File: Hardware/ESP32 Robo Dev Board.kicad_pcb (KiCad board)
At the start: 4 copper layers, 60 x 60 mm, 67 parts, among them J1 USB_C_Receptacle_USB2.0, J2 Conn_01x02_Pin, Q1 DMP2045U, SW1 SW_Push_Dual_x2, U1 ESP32-S3-WROOM-1, U2 TCA9548ARGER, U4 STSPIN250, U5 STSPIN250, U6 USBLC6-2P6, U8 MCP73831-2-OT, U9 AP2112K-3.3

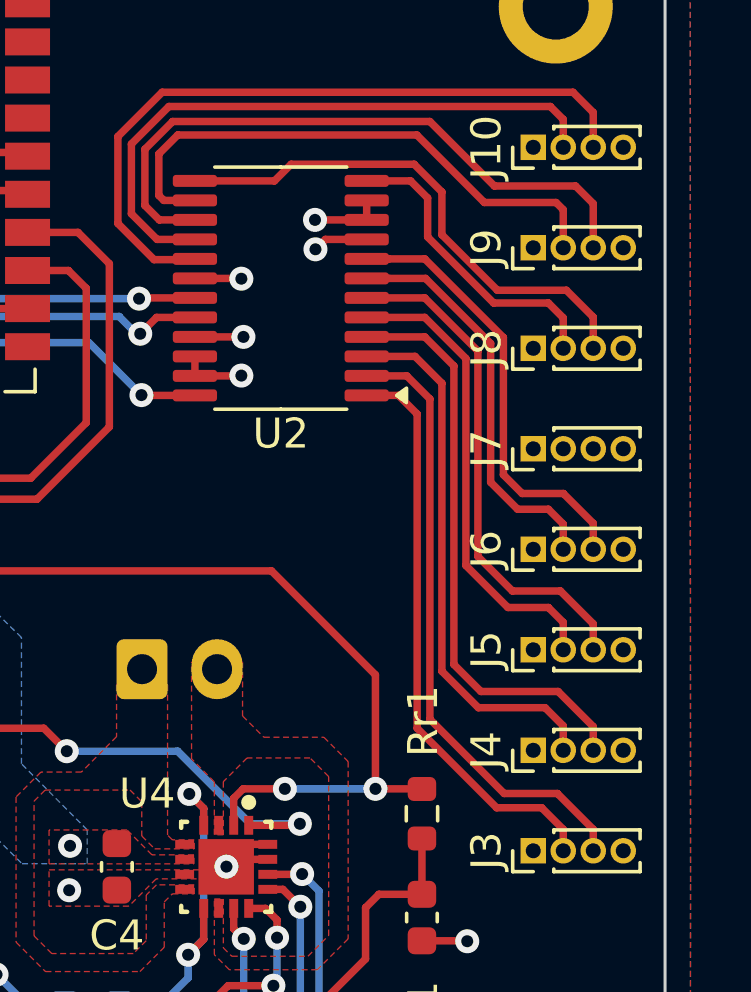
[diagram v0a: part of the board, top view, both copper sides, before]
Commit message: Update I2C Bus Connections
Channel 4 of I2C was not connected, will make traces pretty later.
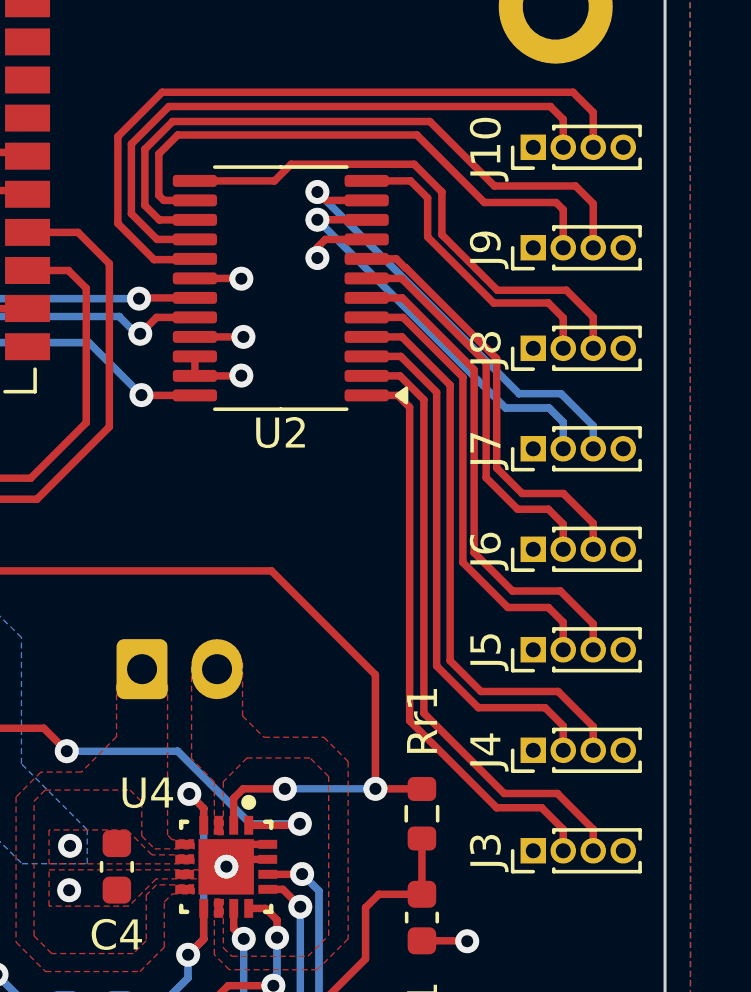
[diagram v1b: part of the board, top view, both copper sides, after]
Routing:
- net /I2C_4C: track 0.00 -> 14.9 mm, vias 0 -> 1
- net /I2C_4D: track 0.00 -> 13.5 mm, vias 0 -> 1
- net GND: track 85.7 -> 83.6 mm, vias 39 -> 38
- net /I2C_3C: track 15.5 -> 14.9 mm

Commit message: Tweaked n' fixed things with @Amoskeag
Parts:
- added Rs2: 18 KΩ, Resistor_SMD:R_0603_1608Metric, F.Cu at (174.2, 81.5)
- added Rs3: 100, Resistor_SMD:R_0603_1608Metric, F.Cu at (174.2, 79.5)
- added SW2: SW_Push, Button_Switch_THT:SW_TH_Tactile_Omron_B3F-100x, F.Cu at (164.5, 78.5)
- moved REF** 42.7 mm to (173.5, 75.0)
- moved G*** 3.45 mm to (152.6, 117.2)
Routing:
- net /Boot: track 0.00 -> 25.8 mm, vias 0 -> 1
- net Net-(Rs3-Pad1): track 0.00 -> 9.64 mm
- net /R_Signal_A: track 2.04 -> 0.00 mm, vias 1 -> 0
- net /R_Signal_B: track 2.00 -> 0.00 mm, vias 1 -> 0
- net /VBAT_DET: track 34.2 -> 35.7 mm
- net GND: vias 38 -> 39
- net +3V3: vias 4 -> 5
- added copper zone on In1.Cu, net +3V3
- removed copper zone on B.Cu, net (none)
- removed copper zone on F.Cu, net (none)

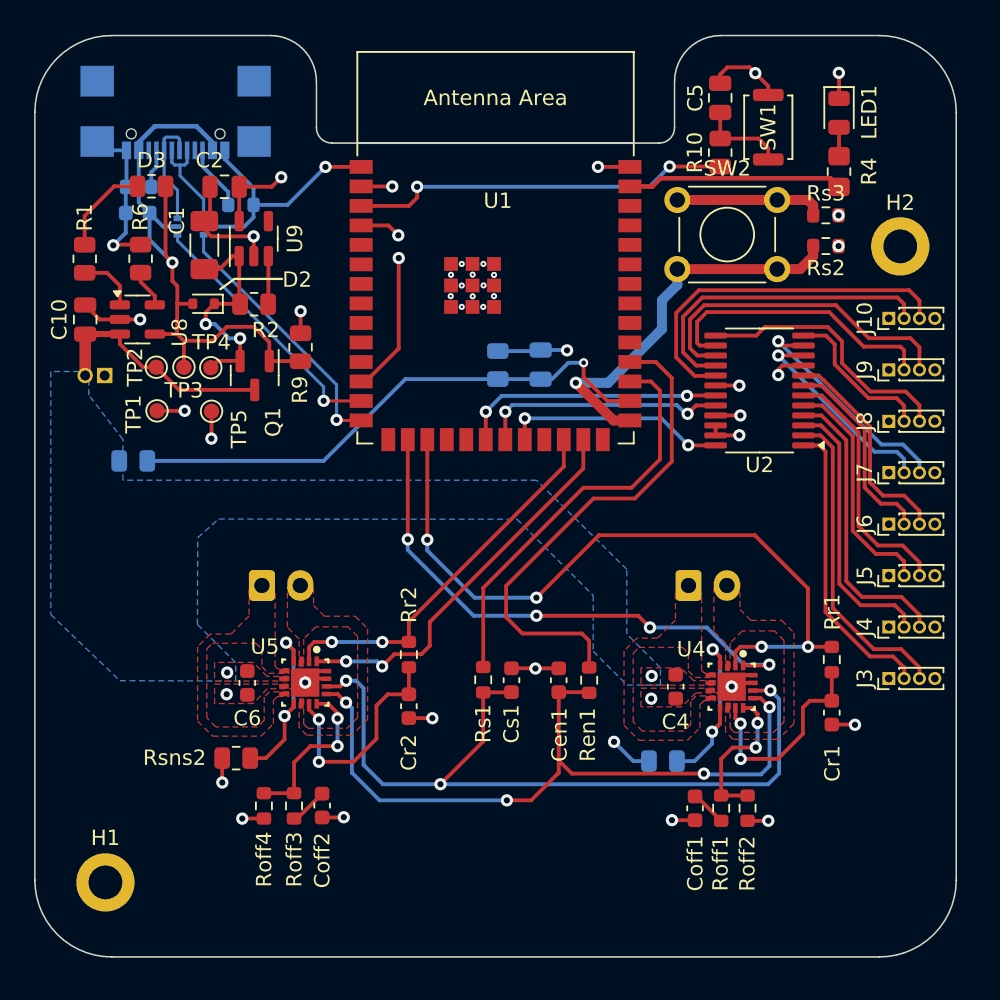
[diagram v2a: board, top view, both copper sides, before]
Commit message: Fix Footprint Targets
Fixed DRC errors on footprints.
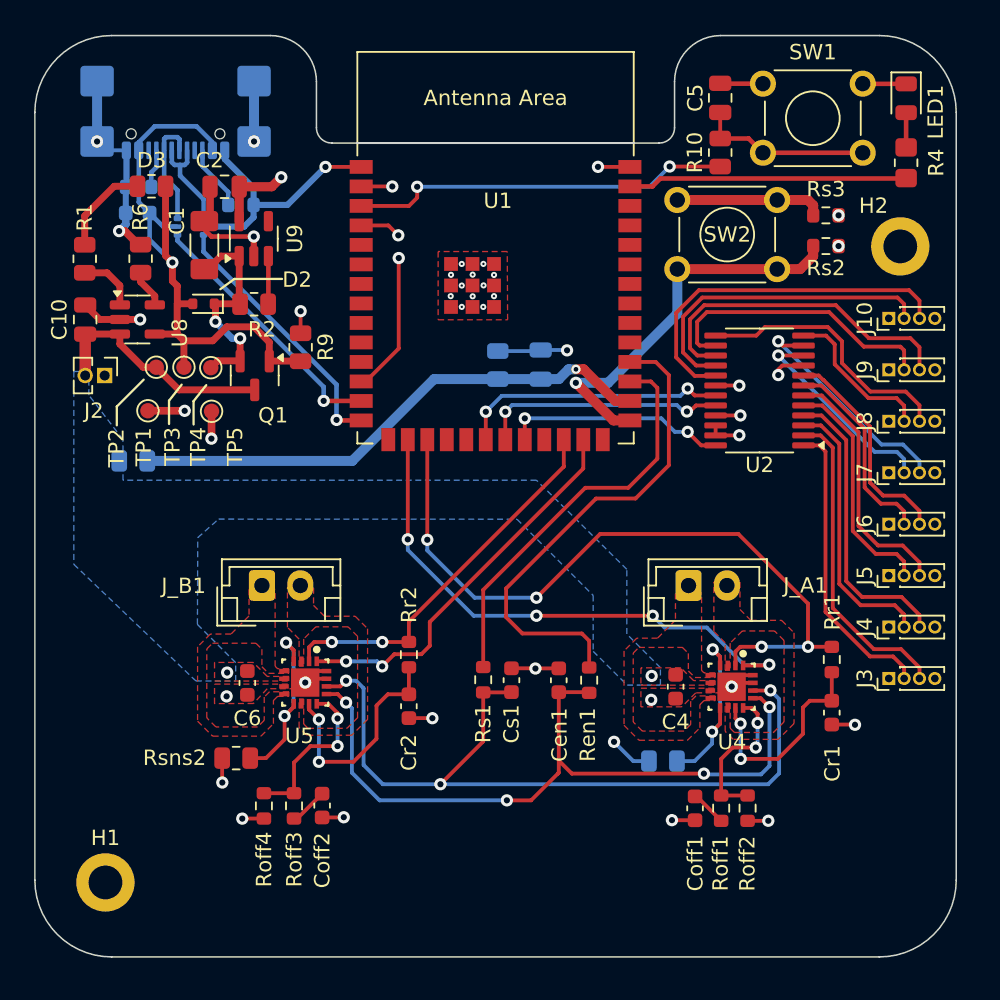
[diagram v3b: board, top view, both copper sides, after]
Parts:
- J1: footprint Amoskeag_KiCAD_Lib:GCT_USB4110GFA -> Connector_USB:USB_C_Receptacle_GCT_USB4110
- J2, J_A1, J_B1: moved to F.Cu
- SW1: footprint Button_Switch_SMD:SW_Push_SPST_NO_Alps_SKRK -> Button_Switch_THT:SW_TH_Tactile_Omron_B3F-100x
- moved REF** 47.1 mm to (176.9, 122.0)
- moved LED1 4.47 mm to (179.4, 71.9)
- moved R4 4.41 mm to (179.4, 76.1)
- moved SW1 2.86 mm to (170.1, 70.9), turned to 0 degrees
- moved J1 2.61 mm to (131.8, 71.6)
- moved G*** 1.82 mm to (152.9, 115.4)
- moved TP1 0.60 mm to (130.0, 92.2)
- turned J2 to -90 degrees
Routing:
- net GND: track 83.6 -> 89.4 mm
- net Net-(SW1A-D): track 5.81 -> 11.4 mm
- net /GPIO1: track 14.1 -> 18.3 mm
- net /VBAT_DET: track 35.7 -> 34.8 mm
- net /V_IN: track 15.2 -> 14.4 mm
- net +3V3: track 10.7 -> 11.3 mm
- net /PWM A: track 47.5 -> 47.0 mm

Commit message: Add JST Connectors for Encoders
Added JST Connectors for my Encoders to attach to.

Fixed all DRC Errors.
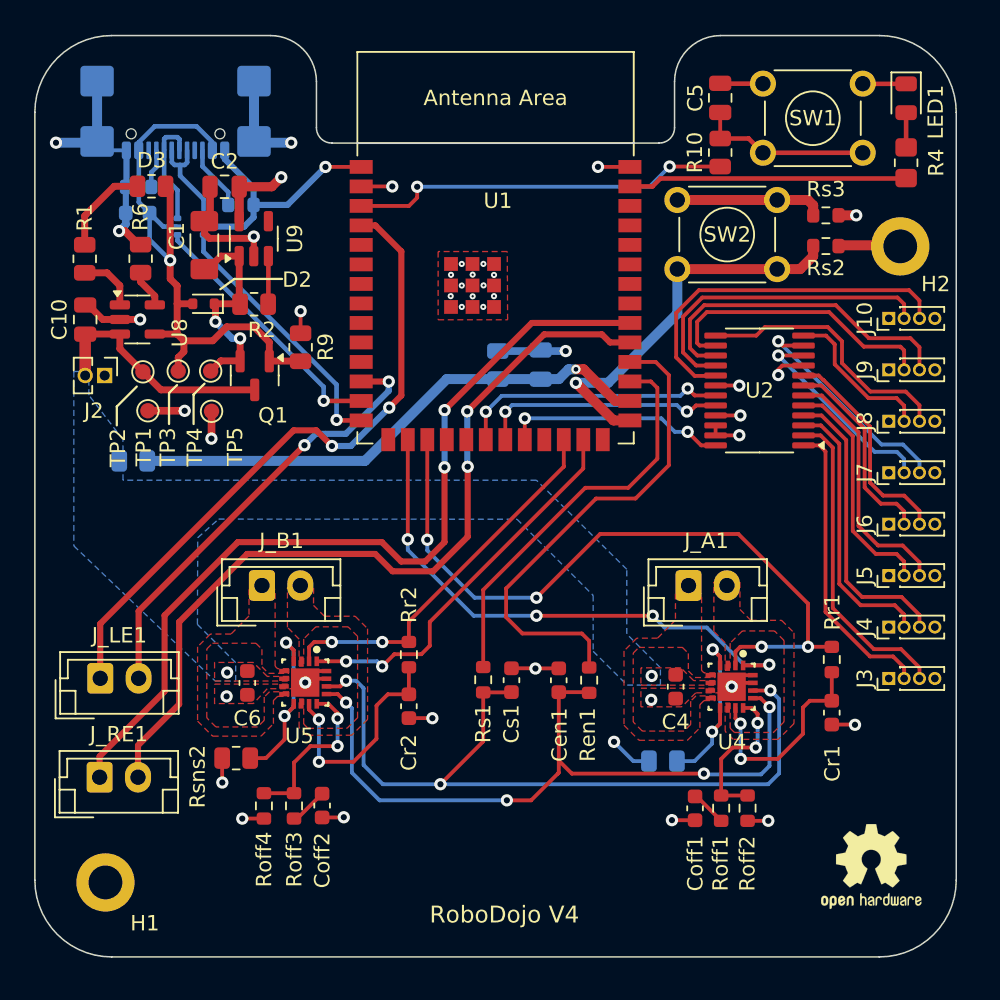
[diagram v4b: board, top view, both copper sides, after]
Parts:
- added J_LE1: Left Encoder, Connector_JST:JST_EH_B2B-EH-A_1x02_P2.50mm_Vertical, F.Cu at (126.9, 109.7)
- added J_RE1: Right Encoder, Connector_JST:JST_EH_B2B-EH-A_1x02_P2.50mm_Vertical, F.Cu at (126.9, 116.1)
- REF**: moved to F.Cu
- moved TP2 0.92 mm to (129.7, 89.7)
- moved TP3 0.45 mm to (132.0, 89.6)
- moved REF** 0.25 mm to (177.1, 121.9), turned to 0 degrees
- moved TP4 0.22 mm to (134.1, 89.6)
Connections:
- U1 pad 31: /R_Signal_B -> /R_Signal_A
- U1 pad 32: /R_Signal_A -> /R_Signal_B
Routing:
- net /R_Signal_B: track 0.00 -> 56.6 mm, vias 0 -> 2
- net /R_Signal_A: track 0.00 -> 54.6 mm, vias 0 -> 2
- net /L_Signal_B: track 2.68 -> 42.9 mm, vias 1 -> 2
- net /L_Signal_A: track 9.23 -> 29.0 mm, vias 1 -> 2
- net GND: track 89.4 -> 98.8 mm, vias 39 -> 38
- net +3V3: track 11.3 -> 12.4 mm
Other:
- board text added: "RoboDojo V4"
- board text removed: "Design By Arthur W. Aznive Jr. https://github.com/Amoskeag/RoboDojo"

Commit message: Increase Trace Widths
Increased the smallest trace width from 0.25 mm to 0.3 mm and beefed up all the other traces.
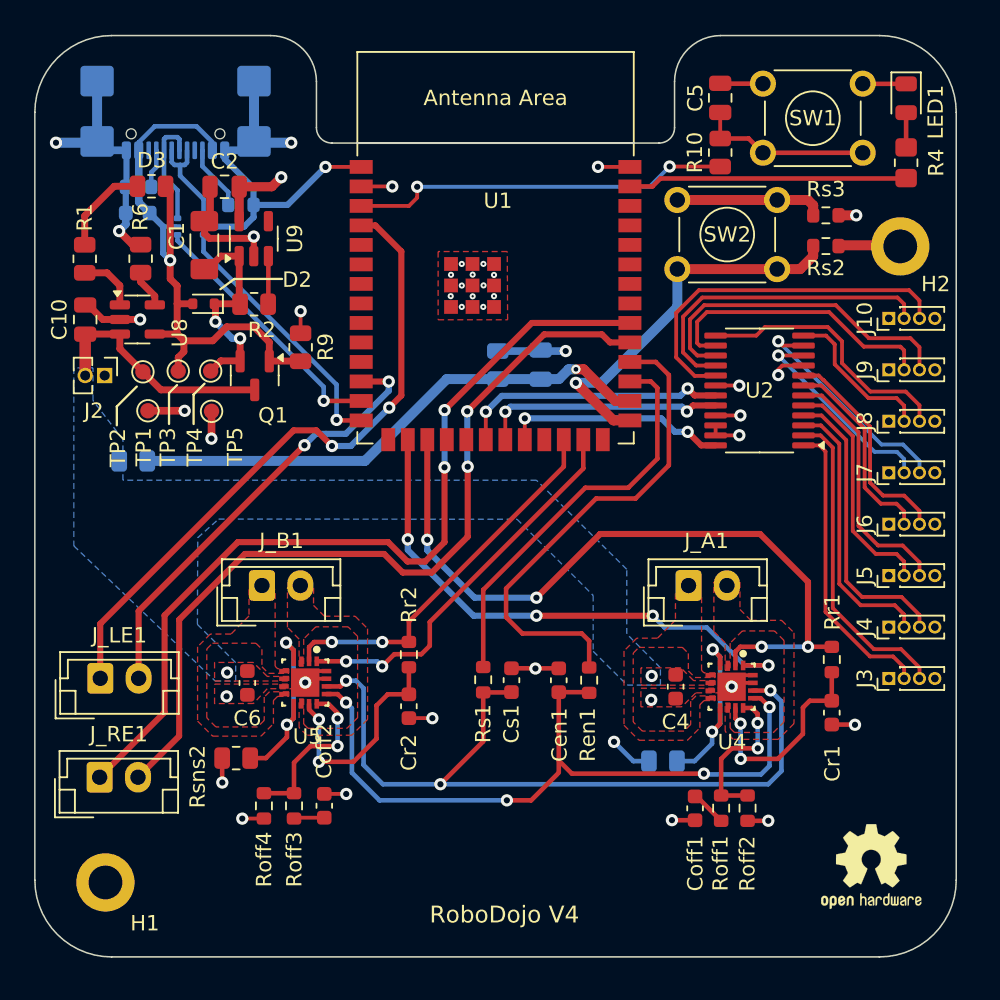
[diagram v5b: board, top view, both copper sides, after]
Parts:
- SW1: value SW_Push_Dual_x2 -> SW1
- moved Coff2 0.14 mm to (141.5, 118.0), turned to 90 degrees
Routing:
- net GND: track 98.8 -> 101.0 mm
- net /V_BUS: track 41.7 -> 40.5 mm
- net /PWM A: track 47.0 -> 47.9 mm
- net /Motor Controller Right/SENSE: track 12.0 -> 12.5 mm

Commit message: Clean Up Schematic
Fixed Schematic notes, and formatting
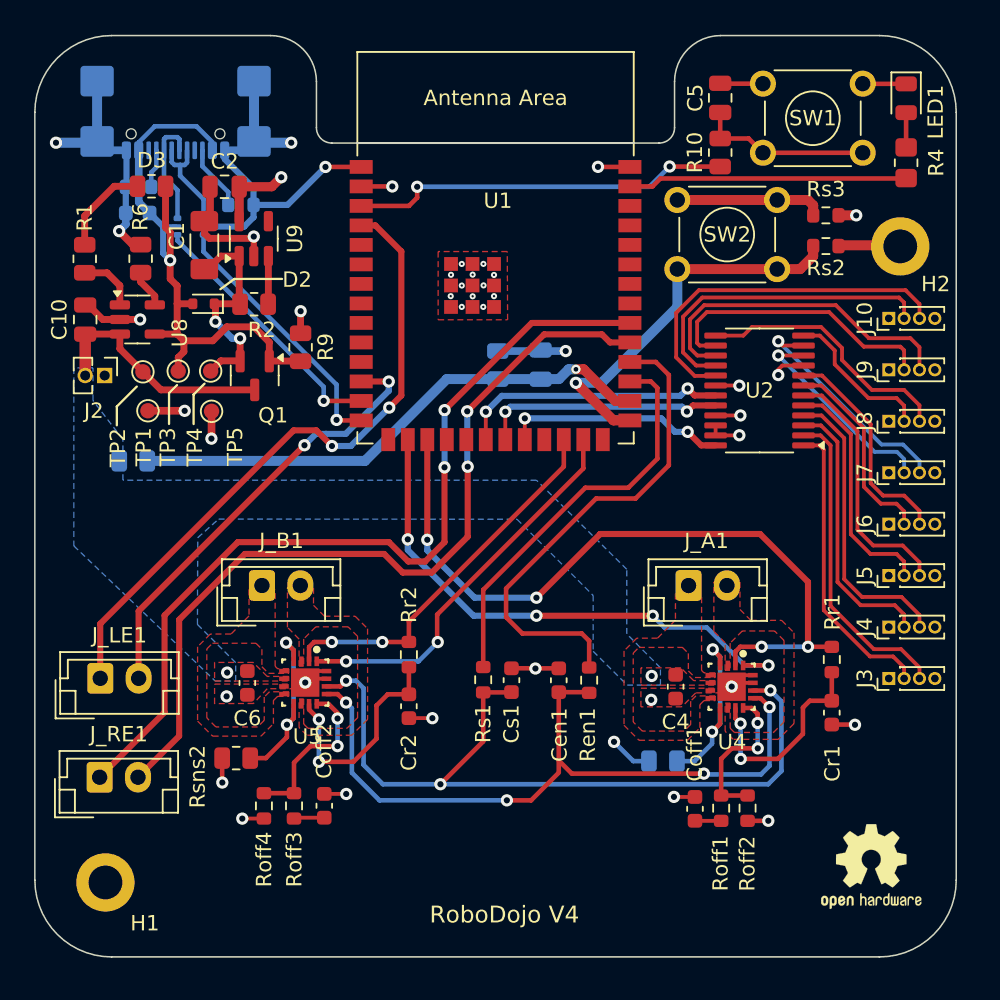
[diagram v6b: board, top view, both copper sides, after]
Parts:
- SW1: value SW1 -> SW_Push_Dual_x2
- turned Coff1 to 90 degrees
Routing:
- net Net-(Coff1-Pad1): track 2.36 -> 1.71 mm
